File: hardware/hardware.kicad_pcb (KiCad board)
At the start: 2 copper layers, 15 parts, among them U1 ESP32-DEVKITC-32D

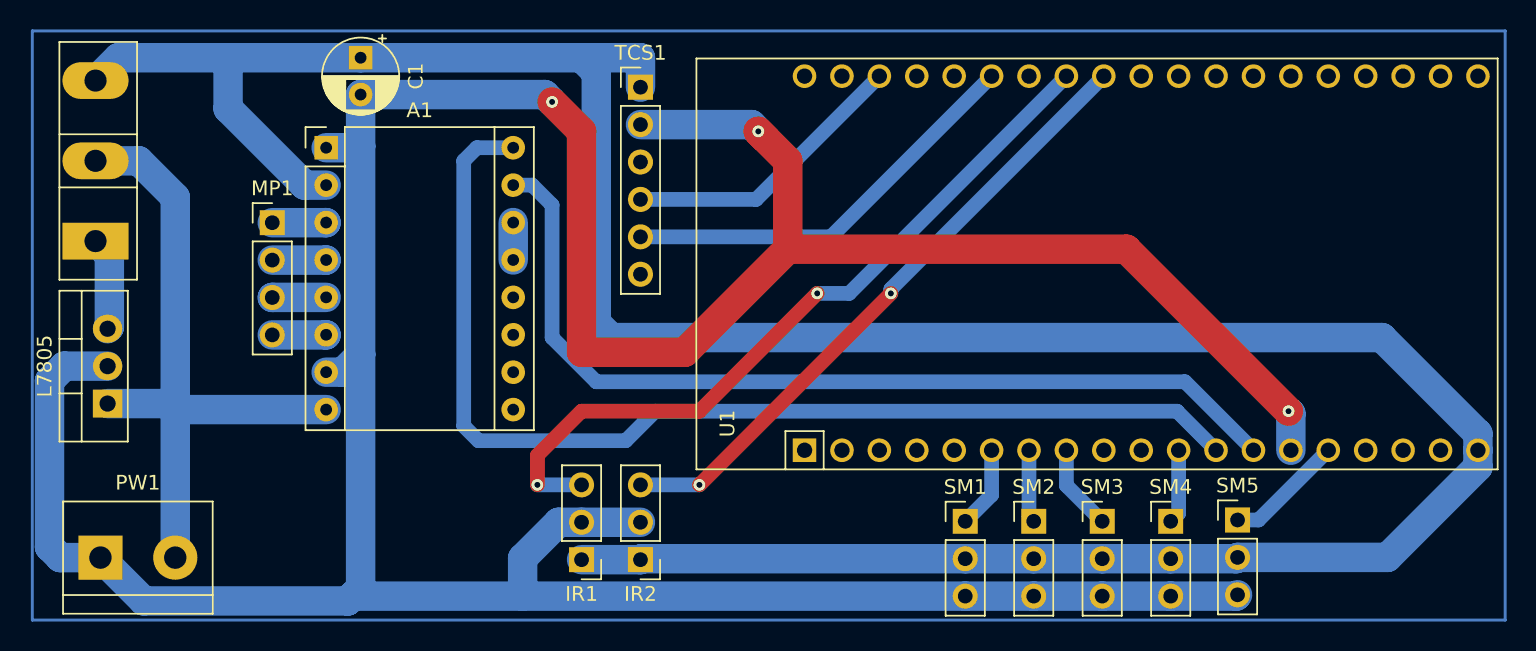
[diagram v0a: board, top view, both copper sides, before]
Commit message: refactor: changed a4988
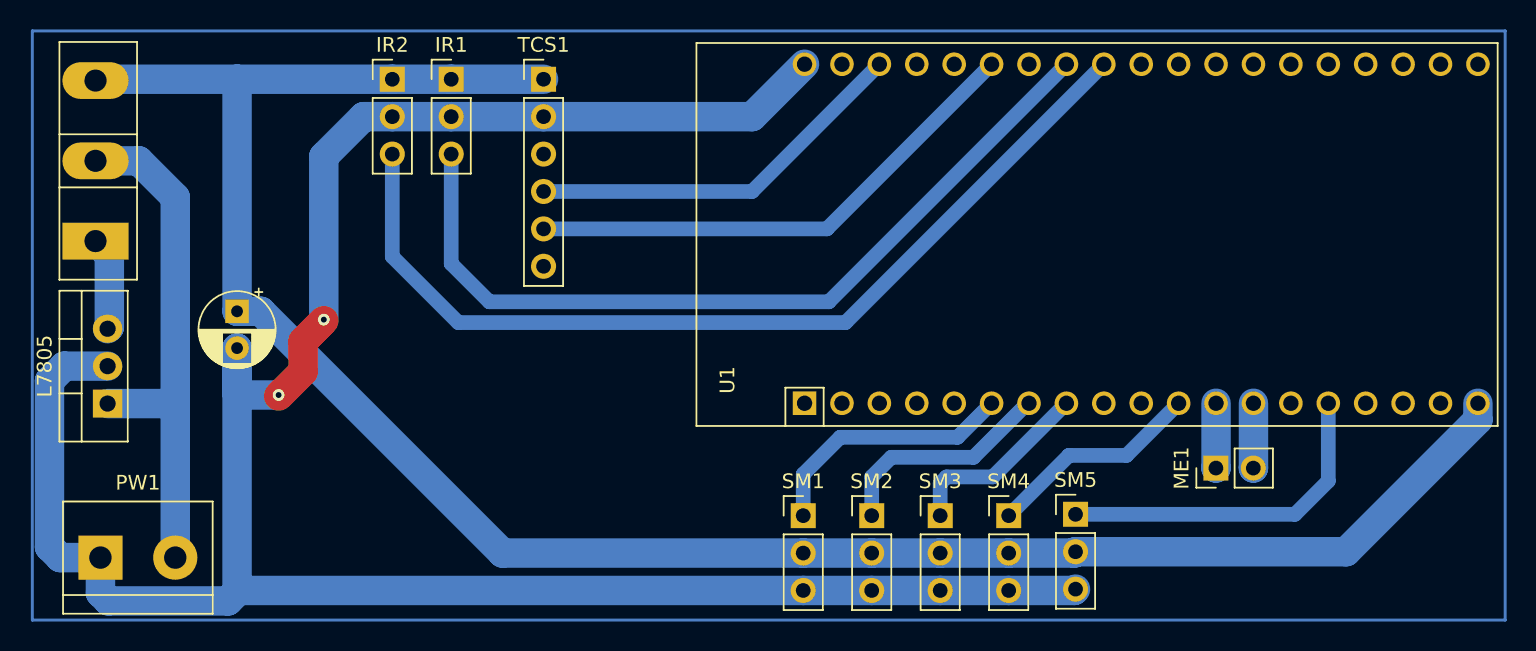
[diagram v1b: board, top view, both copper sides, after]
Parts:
- removed A1: Pololu_Breakout_A4988, Module:Pololu_Breakout-16_15.2x20.3mm
- removed MP1: Conn_01x04_Pin, Connector_PinHeader_2.54mm:PinHeader_1x04_P2.54mm_Vertical
- added ME1: Conn_01x02_Pin, Connector_PinHeader_2.54mm:PinHeader_1x02_P2.54mm_Vertical, F.Cu at (234.1, 108.9)
- moved IR2 36.7 mm to (178.2, 82.5), turned to 0 degrees
- moved IR1 33.8 mm to (182.2, 82.5), turned to 0 degrees
- moved C1 19.2 mm to (167.6, 98.2)
- moved SM1 11.0 mm to (206.1, 112.1)
- moved SM2 11.0 mm to (210.7, 112.1)
- moved SM3 11.0 mm to (215.3, 112.1)
- moved SM4 11.0 mm to (220.0, 112.1)
- moved SM5 11.0 mm to (224.5, 112.0)
- moved TCS1 6.60 mm to (188.4, 82.5)
- moved U1 2.95 mm to (206.1, 104.7)
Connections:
- U1 pad 20: (no net) -> Net-(IR1-Pin_2)
- U1 pad 26: (no net) -> Net-(IR1-Pin_2)
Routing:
- net Net-(IR1-Pin_2): track 256.5 -> 163.7 mm, vias 3 -> 2
- net Net-(ME1-Pin_1): track 75.1 -> 4.40 mm
- net Net-(ME1-Pin_2): track 63.0 -> 4.40 mm
- net Net-(IR1-Pin_1): track 199.0 -> 142.1 mm
- net Net-(IR2-Pin_3): track 43.1 -> 64.4 mm, vias 2 -> 0
- net Net-(SM5-Pin_1): track 8.12 -> 23.4 mm
- net Net-(SM1-Pin_1): track 5.57 -> 17.6 mm
- net Net-(SM2-Pin_1): track 4.96 -> 15.4 mm
- net Net-(L7805-IN): track 46.0 -> 35.7 mm
- net Net-(SM4-Pin_1): track 5.05 -> 14.7 mm
- net Net-(SM3-Pin_1): track 5.83 -> 13.0 mm
- net Net-(TCS1-Pin_5): track 28.4 -> 35.1 mm
- net Net-(TCS1-Pin_4): track 19.7 -> 26.4 mm
- net Net-(IR1-Pin_3): track 51.6 -> 57.0 mm, vias 2 -> 0
- net Net-(A1-2A): track 3.66 -> 0.00 mm
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
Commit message: fix: login
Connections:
- U1 pad 35: (no net) -> Net-(SM1-Pin_1)
- U1 pad 6: Net-(SM1-Pin_1) -> (no net)
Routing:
- net Net-(SM1-Pin_1): track 17.6 -> 63.8 mm
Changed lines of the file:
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@@
     (pad "4" thru_hole circle (at 0.241 7.62 90) (size 1.6 1.6) (drill 1.04) (layers "*.Cu" "*.Mask"))
     (pad "5" thru_hole circle (at 0.241 10.16 90) (size 1.6 1.6) (drill 1.04) (layers "*.Cu" "*.Mask"))
-    (pad "6" thru_hole circle (at 0.241 12.7 90) (size 1.6 1.6) (drill 1.04) (layers "*.Cu" "*.Mask")
-      (net 5 "Net-(SM1-Pin_1)"))
+    (pad "6" thru_hole circle (at 0.241 12.7 90) (size 1.6 1.6) (drill 1.04) (layers "*.Cu" "*.Mask"))
     (pad "7" thru_hole circle (at 0.241 15.24 90) (size 1.6 1.6) (drill 1.04) (layers "*.Cu" "*.Mask")
       (net 6 "Net-(SM2-Pin_1)"))
@@
     (pad "33" thru_hole circle (at 23.26 33.02 90) (size 1.6 1.6) (drill 1.04) (layers "*.Cu" "*.Mask"))
     (pad "34" thru_hole circle (at 23.26 35.56 90) (size 1.6 1.6) (drill 1.04) (layers "*.Cu" "*.Mask"))
-    (pad "35" thru_hole circle (at 23.26 38.1 90) (size 1.6 1.6) (drill 1.04) (layers "*.Cu" "*.Mask"))
+    (pad "35" thru_hole circle (at 23.26 38.1 90) (size 1.6 1.6) (drill 1.04) (layers "*.Cu" "*.Mask")
+      (net 5 "Net-(SM1-Pin_1)"))
     (pad "36" thru_hole circle (at 23.26 40.64 90) (size 1.6 1.6) (drill 1.04) (layers "*.Cu" "*.Mask"))
     (pad "37" thru_hole circle (at 23.26 43.18 90) (size 1.6 1.6) (drill 1.04) (layers "*.Cu" "*.Mask"))
@@
   (segment (start 158.94 94.39) (end 158.94 99.28) (width 2) (layer "B.Cu") (net 4))
   (segment (start 158.94 99.28) (end 158.82 99.4) (width 2) (layer "B.Cu") (net 4))
-  (segment (start 216.5295 106.77) (end 208.56 106.77) (width 1) (layer "B.Cu") (net 5))
-  (segment (start 218.84 104.4595) (end 216.5295 106.77) (width 1) (layer "B.Cu") (net 5))
-  (segment (start 208.56 106.77) (end 206.05 109.28) (width 1) (layer "B.Cu") (net 5))
-  (segment (start 206.05 109.28) (end 206.05 112.09) (width 1) (layer "B.Cu") (net 5))
-  (segment (start 221.283444 104.4595) (end 217.612944 108.13) (width 1) (layer "B.Cu") (net 6))
-  (segment (start 212.0295 108.13) (end 210.7 109.4595) (width 1) (layer "B.Cu") (net 6))
+  (segment (start 224.3705 101.31) (end 201.39 101.31) (width 1) (layer "B.Cu") (net 5))
+  (segment (start 201.39 107.43) (end 206.05 112.09) (width 1) (layer "B.Cu") (net 5))
+  (segment (start 201.39 101.31) (end 201.39 107.43) (width 1) (layer "B.Cu") (net 5))
+  (segment (start 244.24 81.4405) (end 224.3705 101.31) (width 1) (layer "B.Cu") (net 5))
+  (segment (start 221.38 104.4595) (end 221.283444 104.4595) (width 1) (layer "B.Cu") (net 6))
   (segment (start 210.7 109.4595) (end 210.7 112.09) (width 1) (layer "B.Cu") (net 6))
-  (segment (start 217.612944 108.13) (end 212.0295 108.13) (width 1) (layer "B.Cu") (net 6))
-  (segment (start 221.38 104.4595) (end 221.283444 104.4595) (width 1) (layer "B.Cu") (net 6))
-  (segment (start 215.78 109.46) (end 215.35 109.89) (width 1) (layer "B.Cu") (net 7))
+  (segment (start 213.0695 107.09) (end 210.7 109.4595) (width 1) (layer "B.Cu") (net 6))
+  (segment (start 221.283444 104.4595) (end 218.652944 107.09) (width 1) (layer "B.Cu") (net 6))
+  (segment (start 218.652944 107.09) (end 213.0695 107.09) (width 1) (layer "B.Cu") (net 6))
+  (segment (start 223.92 104.4595) (end 219.4695 108.91) (width 1) (layer "B.Cu") (net 7))
   (segment (start 215.35 109.89) (end 215.35 112.09) (width 1) (layer "B.Cu") (net 7))
-  (segment (start 218.9195 109.46) (end 215.78 109.46) (width 1) (layer "B.Cu") (net 7))
-  (segment (start 223.92 104.4595) (end 218.9195 109.46) (width 1) (layer "B.Cu") (net 7))
+  (segment (start 216.33 108.91) (end 215.35 109.89) (width 1) (layer "B.Cu") (net 7))
+  (segment (start 219.4695 108.91) (end 216.33 108.91) (width 1) (layer "B.Cu") (net 7))
   (segment (start 231.54 104.4595) (end 227.9995 108) (width 1) (layer "B.Cu") (net 8))
   (segment (start 227.9995 108) (end 224.09 108) (width 1) (layer "B.Cu") (net 8))
